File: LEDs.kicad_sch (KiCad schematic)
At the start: 102 parts, among them J1 USB C, J2 UART, J3 LEDs, Q1 G30N03D3, Q10 SI2303, Q11 BSS138, Q12 BSS138, Q13 BSS138, Q2 G30N03D3, Q3 BSS138, Q4 BSS138, Q5 SI2303, Q6 BSS138, Q7 BSS138, Q8 AO4407C, Q9 BSS138, SW1 4-pin, U1 TP4056, U2 DW01A, U3 MT3608, U4 MT3608, U5 ESP32-C3-WROOM-02, U6 AMS1117-3.3, U7 DS18B20, U8 LM358S, U9 TUSB321

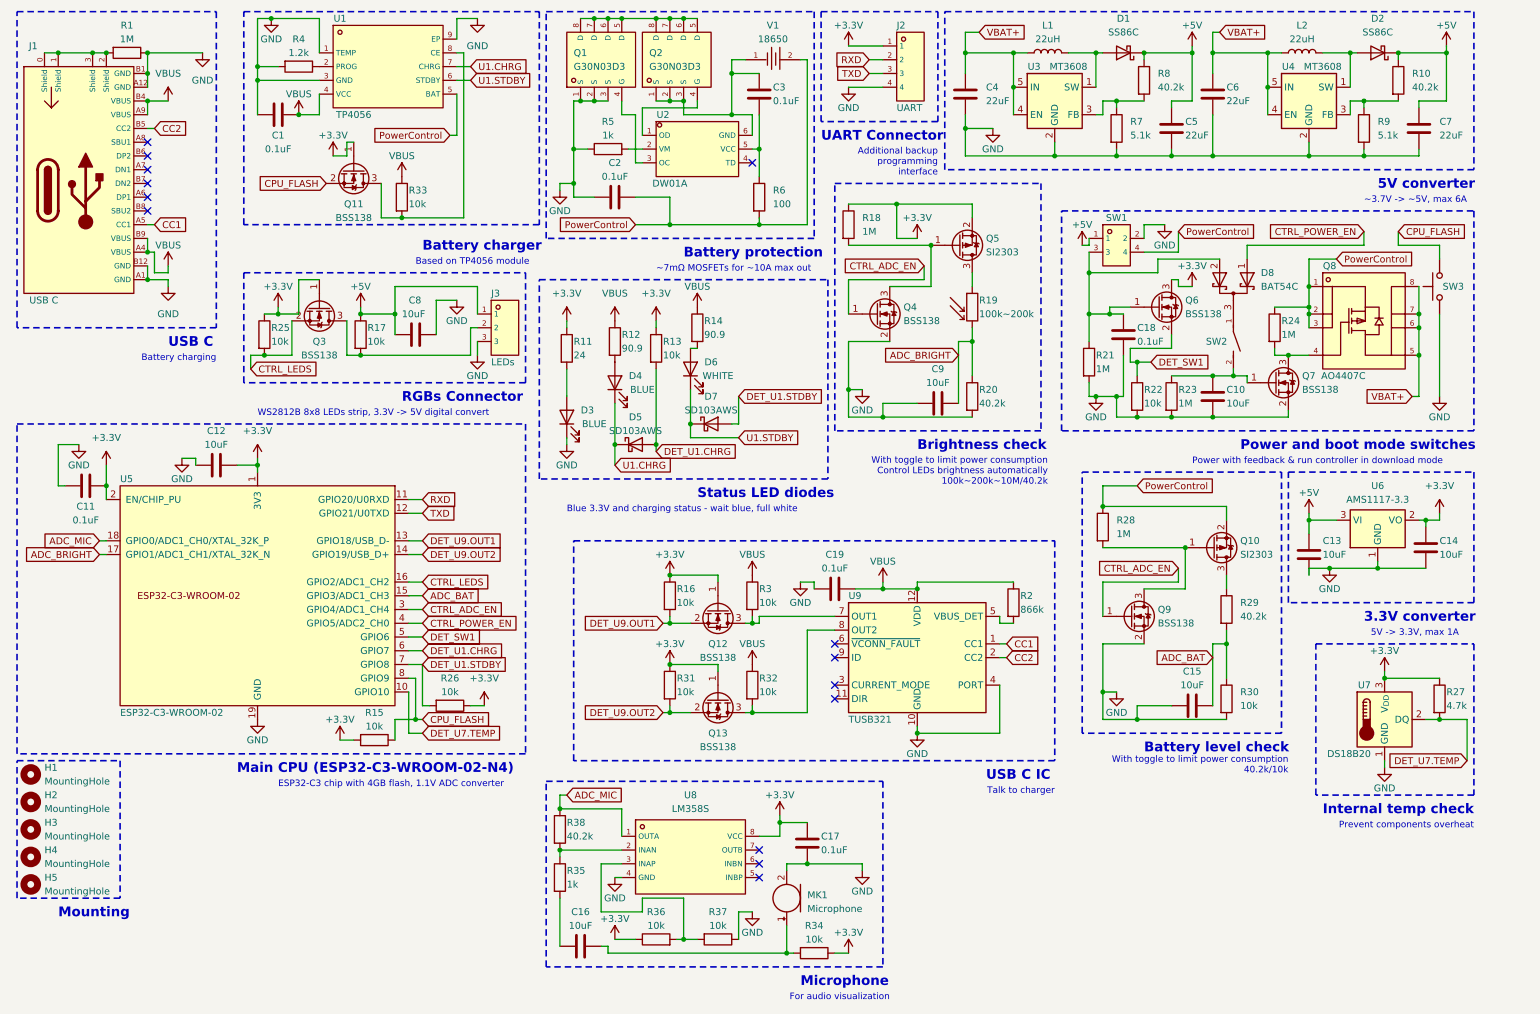
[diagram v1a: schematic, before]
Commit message: Small resistor change
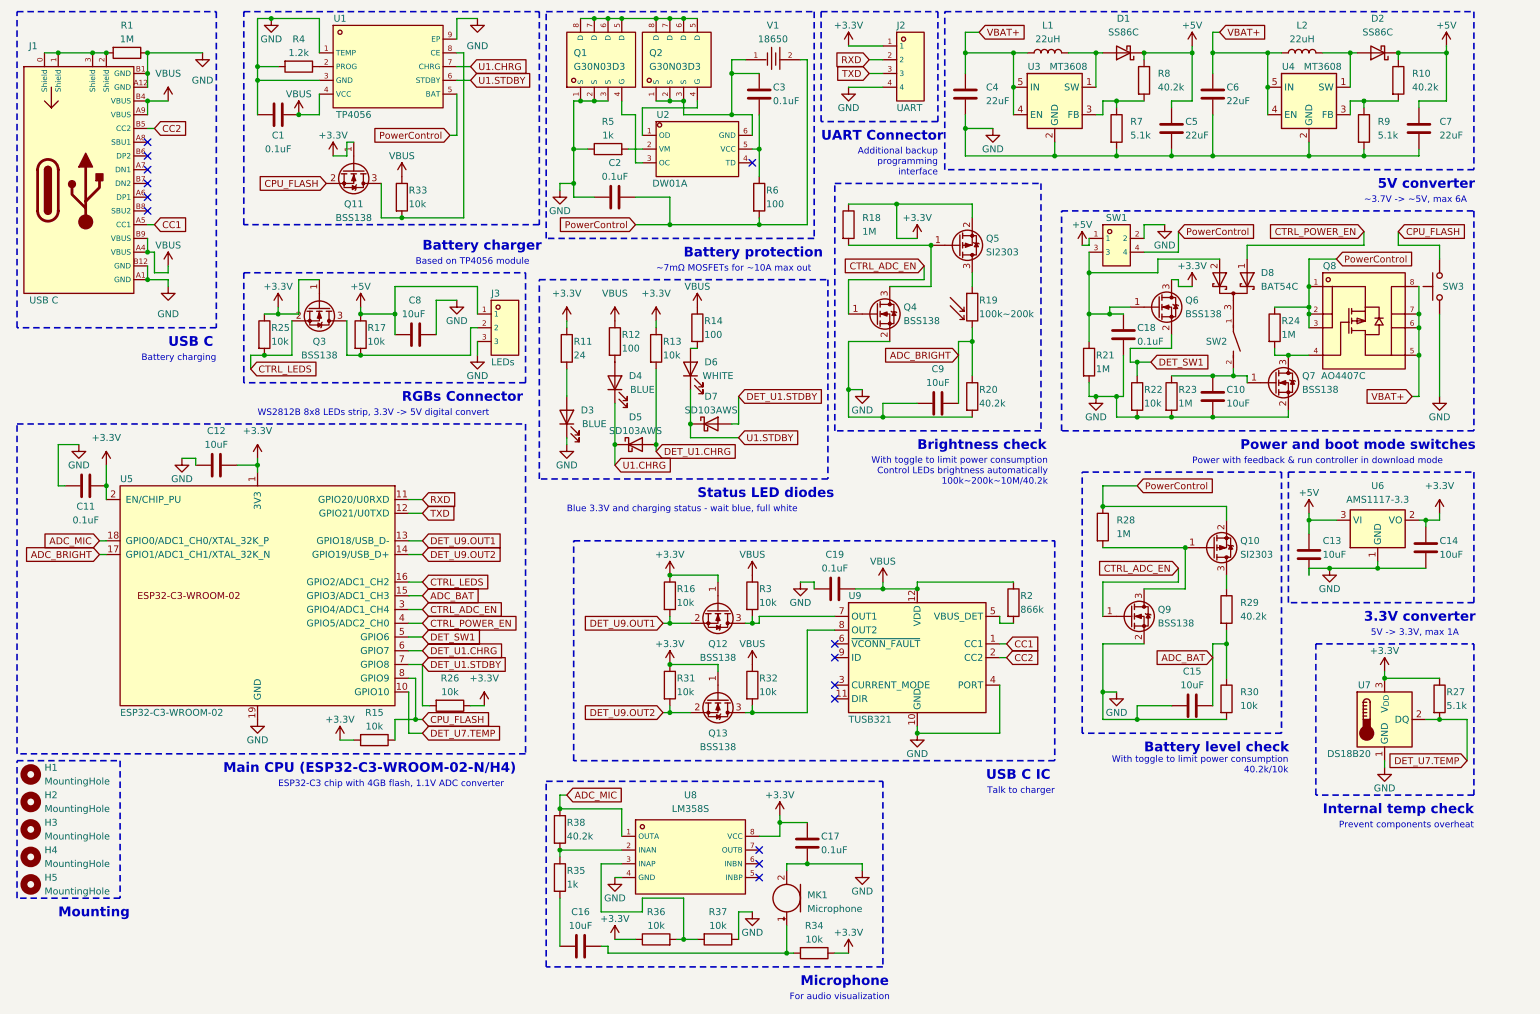
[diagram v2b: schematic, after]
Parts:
- removed R12, R14: 90.9, Resistor_SMD:R_0603_1608Metric_Pad0.98x0.95mm_HandSolder, symbol Resistors:R-82-100mW
- removed R27: 4.7k, Resistor_SMD:R_0603_1608Metric_Pad0.98x0.95mm_HandSolder, symbol Device:R
- added R12, R14: 100, Resistor_SMD:R_0603_1608Metric_Pad0.98x0.95mm_HandSolder, symbol Resistors:R-100-100mW
- added R27: 5.1k, Resistor_SMD:R_0603_1608Metric_Pad0.98x0.95mm_HandSolder, symbol Resistors:R-5.1k-100mW
- U5: LCSC C2934560 -> C2944070
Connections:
- net +3.3V: now also R27.1
- net DET_U7.TEMP: now also R27.2
- net VBUS: now also R12.1, R14.1
- net at D6.2 (A): now also R14.2
- net at D4.2 (A): now also R12.2
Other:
- note added: "Main CPU (ESP32-C3-WROOM-02-N/H4)"
- note removed: "Main CPU (ESP32-C3-WROOM-02-N4)"
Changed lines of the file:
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@@
   (junction (at 238.76 81.28) (diameter 0) (color 0 0 0 0)
   )
+  (junction (at 276.86 144.78) (diameter 0) (color 0 0 0 0)
+  )
   (junction (at 66.04 33.02) (diameter 0) (color 0 0 0 0)
   )
@@
   (junction (at 123.19 15.24) (diameter 0) (color 0 0 0 0)
   )
-  (junction (at 276.86 144.78) (diameter 0) (color 0 0 0 0)
-  )
   (junction (at 266.7 137.16) (diameter 0) (color 0 0 0 0)
   )
@@
     (stroke (width 0) (type default))
   )
+  (wire (pts (xy 276.86 144.78) (xy 281.94 144.78))
+    (stroke (width 0) (type default))
+  )
   (wire (pts (xy 58.42 24.13) (xy 58.42 26.67))
     (stroke (width 0) (type default))
@@
     (stroke (width 0) (type default))
   )
-  (wire (pts (xy 281.94 144.78) (xy 276.86 144.78))
-    (stroke (width 0) (type default))
-  )
   (wire (pts (xy 99.06 64.77) (xy 99.06 69.85))
     (stroke (width 0) (type default))
@@
     (effects (font (size 1.2 1.2) (color 132 0 0 1)) (justify left bottom))
   )
-  (text "Main CPU (ESP32-C3-WROOM-02-N4)" (at 54.61 154.94 0)
+  (text "Main CPU (ESP32-C3-WROOM-02-N/H4)" (at 52.07 154.94 0)
     (effects (font (size 1.8 1.8) (thickness 0.36) bold (color 0 194 194 1)) (justify left bottom))
   )
@@
     )
   )
-  (symbol (lib_id "Device:R") (at 276.86 140.97 0) (unit 1)
-    (in_bom yes) (on_board yes) (dnp no)
-    (property "Reference" "R27" (at 278.13 139.7 0)
-      (effects (font (size 1.27 1.27)) (justify left))
-    )
-    (property "Value" "4.7k" (at 278.13 142.24 0)
-      (effects (font (size 1.27 1.27)) (justify left))
-    )
-    (property "Footprint" "Resistor_SMD:R_0603_1608Metric_Pad0.98x0.95mm_HandSolder" (at 275.082 140.97 90)
-      (effects (font (size 1.27 1.27)) hide)
-    )
-    (property "Datasheet" "~" (at 276.86 140.97 0)
-      (effects (font (size 1.27 1.27)) hide)
-    )
-    (property "LCSC" "C3017722" (at 276.86 140.97 0)
-      (effects (font (size 1.27 1.27)) hide)
-    )
-    (pin "1")
-    (pin "2")
-    (instances
-      (project "LEDs"
-        (path "/d01d2d57-eea2-4c74-9646-8b66fde96c25"
-          (reference "R27") (unit 1)
-        )
-      )
-    )
-  )
   (symbol (lib_id "Resistors:R-1k-100mW") (at 114.3 173.99 0) (unit 1)
     (in_bom yes) (on_board yes) (dnp no)
@@
     )
   )
-  (symbol (lib_id "Resistors:R-82-100mW") (at 139.7 72.39 0) (unit 1)
-    (in_bom yes) (on_board yes) (dnp no)
-    (property "Reference" "R14" (at 140.97 71.12 0)
-      (effects (font (size 1.27 1.27)) (justify left))
-    )
-    (property "Value" "90.9" (at 140.97 73.66 0)
-      (effects (font (size 1.27 1.27)) (justify left))
-    )
-    (property "Footprint" "Resistor_SMD:R_0603_1608Metric_Pad0.98x0.95mm_HandSolder" (at 137.922 72.39 90)
-      (effects (font (size 1.27 1.27)) hide)
-    )
-    (property "Datasheet" "~" (at 139.7 72.39 0)
-      (effects (font (size 1.27 1.27)) hide)
-    )
-    (property "LCSC" "C101232" (at 139.7 72.39 0)
-      (effects (font (size 1.27 1.27)) hide)
-    )
-    (pin "1")
-    (pin "2")
-    (instances
-      (project "LEDs"
-        (path "/d01d2d57-eea2-4c74-9646-8b66fde96c25"
-          (reference "R14") (unit 1)
-        )
-      )
-    )
-  )
   (symbol (lib_id "Device:LED") (at 124.46 82.55 90) (unit 1)
     (in_bom yes) (on_board yes) (dnp no)
@@
     )
   )
+  (symbol (lib_id "Resistors:R-100-100mW") (at 139.7 72.39 0) (unit 1)
+    (in_bom yes) (on_board yes) (dnp no)
+    (property "Reference" "R14" (at 140.97 71.12 0)
+      (effects (font (size 1.27 1.27)) (justify left))
+    )
+    (property "Value" "100" (at 140.97 73.66 0)
+      (effects (font (size 1.27 1.27)) (justify left))
+    )
+    (property "Footprint" "Resistor_SMD:R_0603_1608Metric_Pad0.98x0.95mm_HandSolder" (at 137.922 72.39 90)
+      (effects (font (size 1.27 1.27)) hide)
+    )
+    (property "Datasheet" "~" (at 139.7 72.39 0)
+      (effects (font (size 1.27 1.27)) hide)
+    )
+    (property "LCSC" "C3017758" (at 139.7 72.39 90)
+      (effects (font (size 1.27 1.27)) hide)
+    )
+    (pin "1")
+    (pin "2")
+    (instances
+      (project "LEDs"
+        (path "/d01d2d57-eea2-4c74-9646-8b66fde96c25"
+          (reference "R14") (unit 1)
+        )
+      )
+    )
+  )
   (symbol (lib_id "Capacitors:C-0.1uF-16V") (at 124.46 48.26 90) (unit 1)
     (in_bom yes) (on_board yes) (dnp no)
@@
   )
   (symbol (lib_id "Resistors:R-100-100mW") (at 151.13 48.26 0) (unit 1)
-    (in_bom yes) (on_board yes) (dnp no) (fields_autoplaced)
-    (property "Reference" "R6" (at 153.67 46.99 0)
+    (in_bom yes) (on_board yes) (dnp no)
+    (property "Reference" "R6" (at 152.4 46.99 0)
       (effects (font (size 1.27 1.27)) (justify left))
     )
-    (property "Value" "100" (at 153.67 49.53 0)
+    (property "Value" "100" (at 152.4 49.53 0)
       (effects (font (size 1.27 1.27)) (justify left))
     )
@@
     )
   )
-  (symbol (lib_id "Resistors:R-82-100mW") (at 124.46 74.93 0) (unit 1)
-    (in_bom yes) (on_board yes) (dnp no)
-    (property "Reference" "R12" (at 125.73 73.66 0)
-      (effects (font (size 1.27 1.27)) (justify left))
-    )
-    (property "Value" "90.9" (at 125.73 76.2 0)
-      (effects (font (size 1.27 1.27)) (justify left))
-    )
-    (property "Footprint" "Resistor_SMD:R_0603_1608Metric_Pad0.98x0.95mm_HandSolder" (at 122.682 74.93 90)
-      (effects (font (size 1.27 1.27)) hide)
-    )
-    (property "Datasheet" "~" (at 124.46 74.93 0)
-      (effects (font (size 1.27 1.27)) hide)
-    )
-    (property "LCSC" "C101232" (at 124.46 74.93 0)
-      (effects (font (size 1.27 1.27)) hide)
-    )
-    (pin "1")
-    (pin "2")
-    (instances
-      (project "LEDs"
-        (path "/d01d2d57-eea2-4c74-9646-8b66fde96c25"
-          (reference "R12") (unit 1)
-        )
-      )
-    )
-  )
   (symbol (lib_id "Device:Microphone") (at 156.21 177.8 180) (unit 1)
     (in_bom yes) (on_board yes) (dnp no) (fields_autoplaced)
@@
     )
   )
+  (symbol (lib_name "R-5.1k-100mW_1") (lib_id "Resistors:R-5.1k-100mW") (at 276.86 140.97 0) (unit 1)
+    (in_bom yes) (on_board yes) (dnp no)
+    (property "Reference" "R27" (at 278.13 139.7 0)
+      (effects (font (size 1.27 1.27)) (justify left))
+    )
+    (property "Value" "5.1k" (at 278.13 142.24 0)
+      (effects (font (size 1.27 1.27)) (justify left))
+    )
+    (property "Footprint" "Resistor_SMD:R_0603_1608Metric_Pad0.98x0.95mm_HandSolder" (at 270.51 140.97 90)
+      (effects (font (size 1.27 1.27)) hide)
+    )
+    (property "Datasheet" "~" (at 276.86 140.97 0)
+      (effects (font (size 1.27 1.27)) hide)
+    )
+    (property "LCSC" "C2907114" (at 284.48 135.89 0)
+      (effects (font (size 1.27 1.27)) hide)
+    )
+    (pin "1")
+    (pin "2")
+    (instances
+      (project "LEDs"
+        (path "/d01d2d57-eea2-4c74-9646-8b66fde96c25"
+          (reference "R27") (unit 1)
+        )
+      )
+    )
+  )
   (symbol (lib_id "power:+3.3V") (at 231.14 64.77 0) (unit 1)
     (in_bom yes) (on_board yes) (dnp no)
@@
       (effects (font (size 1.27 1.27)) hide)
     )
-    (property "LCSC" "C2934560" (at 58.42 121.92 0)
+    (property "LCSC" "C2944070" (at 58.42 121.92 0)
       (effects (font (size 1.27 1.27)) hide)
     )
@@
         )
       )
+    )
+  )
+  (symbol (lib_id "Resistors:R-100-100mW") (at 124.46 74.93 0) (unit 1)
+    (in_bom yes) (on_board yes) (dnp no)
+    (property "Reference" "R12" (at 125.73 73.66 0)
+      (effects (font (size 1.27 1.27)) (justify left))
+    )
+    (property "Value" "100" (at 125.73 76.2 0)
+      (effects (font (size 1.27 1.27)) (justify left))
+    )
+    (property "Footprint" "Resistor_SMD:R_0603_1608Metric_Pad0.98x0.95mm_HandSolder" (at 122.682 74.93 90)
+      (effects (font (size 1.27 1.27)) hide)
+    )
+    (property "Datasheet" "~" (at 124.46 74.93 0)
+      (effects (font (size 1.27 1.27)) hide)
+    )
+    (property "LCSC" "C3017758" (at 124.46 74.93 90)
+      (effects (font (size 1.27 1.27)) hide)
+    )
+    (pin "1")
+    (pin "2")
+    (instances
+      (project "LEDs"
+        (path "/d01d2d57-eea2-4c74-9646-8b66fde96c25"
+          (reference "R12") (unit 1)
+        )
+      )

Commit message: Changes
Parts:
- H1, H2, H3, H4, H5: now left out of the parts list
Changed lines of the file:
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@@
   )
   (symbol (lib_id "Mechanical:MountingHole") (at 16.51 165.1 0) (unit 1)
-    (in_bom yes) (on_board yes) (dnp no) (fields_autoplaced)
+    (in_bom no) (on_board no) (dnp no) (fields_autoplaced)
     (property "Reference" "H3" (at 19.05 163.83 0)
       (effects (font (size 1.27 1.27)) (justify left))
@@
   )
   (symbol (lib_id "Mechanical:MountingHole") (at 16.51 160.02 0) (unit 1)
-    (in_bom yes) (on_board yes) (dnp no) (fields_autoplaced)
+    (in_bom no) (on_board no) (dnp no) (fields_autoplaced)
     (property "Reference" "H2" (at 19.05 158.75 0)
       (effects (font (size 1.27 1.27)) (justify left))
@@
   )
   (symbol (lib_id "Mechanical:MountingHole") (at 16.51 154.94 0) (unit 1)
-    (in_bom yes) (on_board yes) (dnp no) (fields_autoplaced)
+    (in_bom no) (on_board no) (dnp no) (fields_autoplaced)
     (property "Reference" "H1" (at 19.05 153.67 0)
       (effects (font (size 1.27 1.27)) (justify left))
@@
   )
   (symbol (lib_id "Mechanical:MountingHole") (at 16.51 170.18 0) (unit 1)
-    (in_bom yes) (on_board yes) (dnp no) (fields_autoplaced)
+    (in_bom no) (on_board no) (dnp no) (fields_autoplaced)
     (property "Reference" "H4" (at 19.05 168.91 0)
       (effects (font (size 1.27 1.27)) (justify left))
@@
   )
   (symbol (lib_id "Mechanical:MountingHole") (at 16.51 175.26 0) (unit 1)
-    (in_bom yes) (on_board yes) (dnp no) (fields_autoplaced)
+    (in_bom no) (on_board no) (dnp no) (fields_autoplaced)
     (property "Reference" "H5" (at 19.05 173.99 0)
       (effects (font (size 1.27 1.27)) (justify left))

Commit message: :p
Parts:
- R5: value 1k -> 1.2k; LCSC C3016283 -> C2907081
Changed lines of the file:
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@@
       (effects (font (size 1.27 1.27)))
     )
-    (property "Value" "1k" (at 123.19 36.83 90)
+    (property "Value" "1.2k" (at 123.19 36.83 90)
       (effects (font (size 1.27 1.27)))
     )
@@
       (effects (font (size 1.27 1.27)) hide)
     )
-    (property "LCSC" "C3016283" (at 123.19 39.37 90)
+    (property "LCSC" "C2907081" (at 123.19 39.37 90)
       (effects (font (size 1.27 1.27)) hide)
     )
